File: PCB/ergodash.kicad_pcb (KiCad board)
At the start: 2 copper layers, 149.9 x 127.4 mm, 183 parts, among them J1 5PIN, J2 Conn_01x03, J3 Conn_01x03, J4 GS3, J5 GS3, Q1 IRLML6344TRPbF, SW1 SW_PUSH, SW10 SW_PUSH, SW11 SW_PUSH, SW12 SW_PUSH, SW13 SW_PUSH, SW14 SW_PUSH, SW15 SW_PUSH, SW16 SW_PUSH, SW17 SW_PUSH, SW18 SW_PUSH, SW19 SW_PUSH, SW2 SW_PUSH, SW20 SW_PUSH, SW21 SW_PUSH, SW22 SW_PUSH, SW23 SW_PUSH, SW24 SW_PUSH, SW25 SW_PUSH, SW26 SW_PUSH, SW27 SW_PUSH, SW28 SW_PUSH, SW29 SW_Push, SW3 SW_PUSH, SW30 SW_PUSH, SW31 SW_PUSH, SW32 SW_PUSH, SW33 SW_PUSH, SW34 SW_PUSH, SW35 SW_PUSH, SW36 SW_PUSH, SW37 SW_Push, SW38 SW_PUSH, SW39 SW_PUSH, SW4 SW_PUSH, SW40 SW_PUSH, SW41 SW_PUSH, SW5 SW_PUSH, SW6 SW_PUSH, SW7 SW_PUSH, SW8 SW_PUSH, SW9 SW_PUSH, U1 HOLE, U2 HOLE, U3 ProMicro, U4 HOLE, U5 HOLE, U6 ProMicro, U7 HOLE, U8 HOLE, U9 HOLE

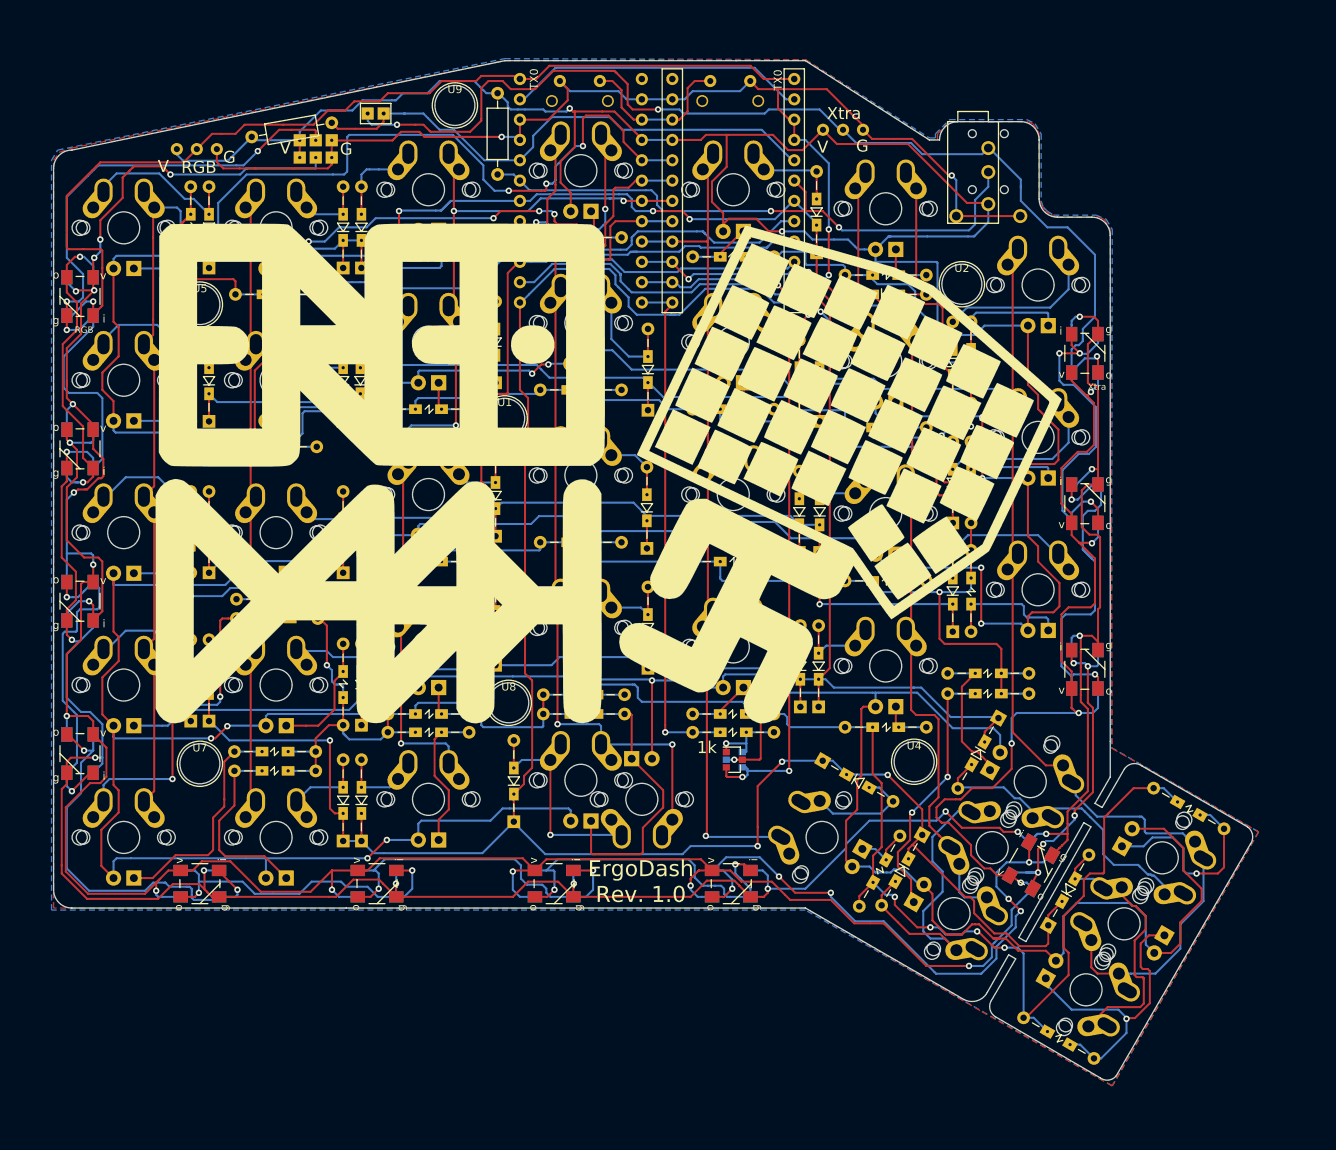
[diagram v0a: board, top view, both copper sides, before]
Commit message: My adpatations added
- Changed TRRS jack to PJ-320A
- Added border and holes for sandwich plateless case
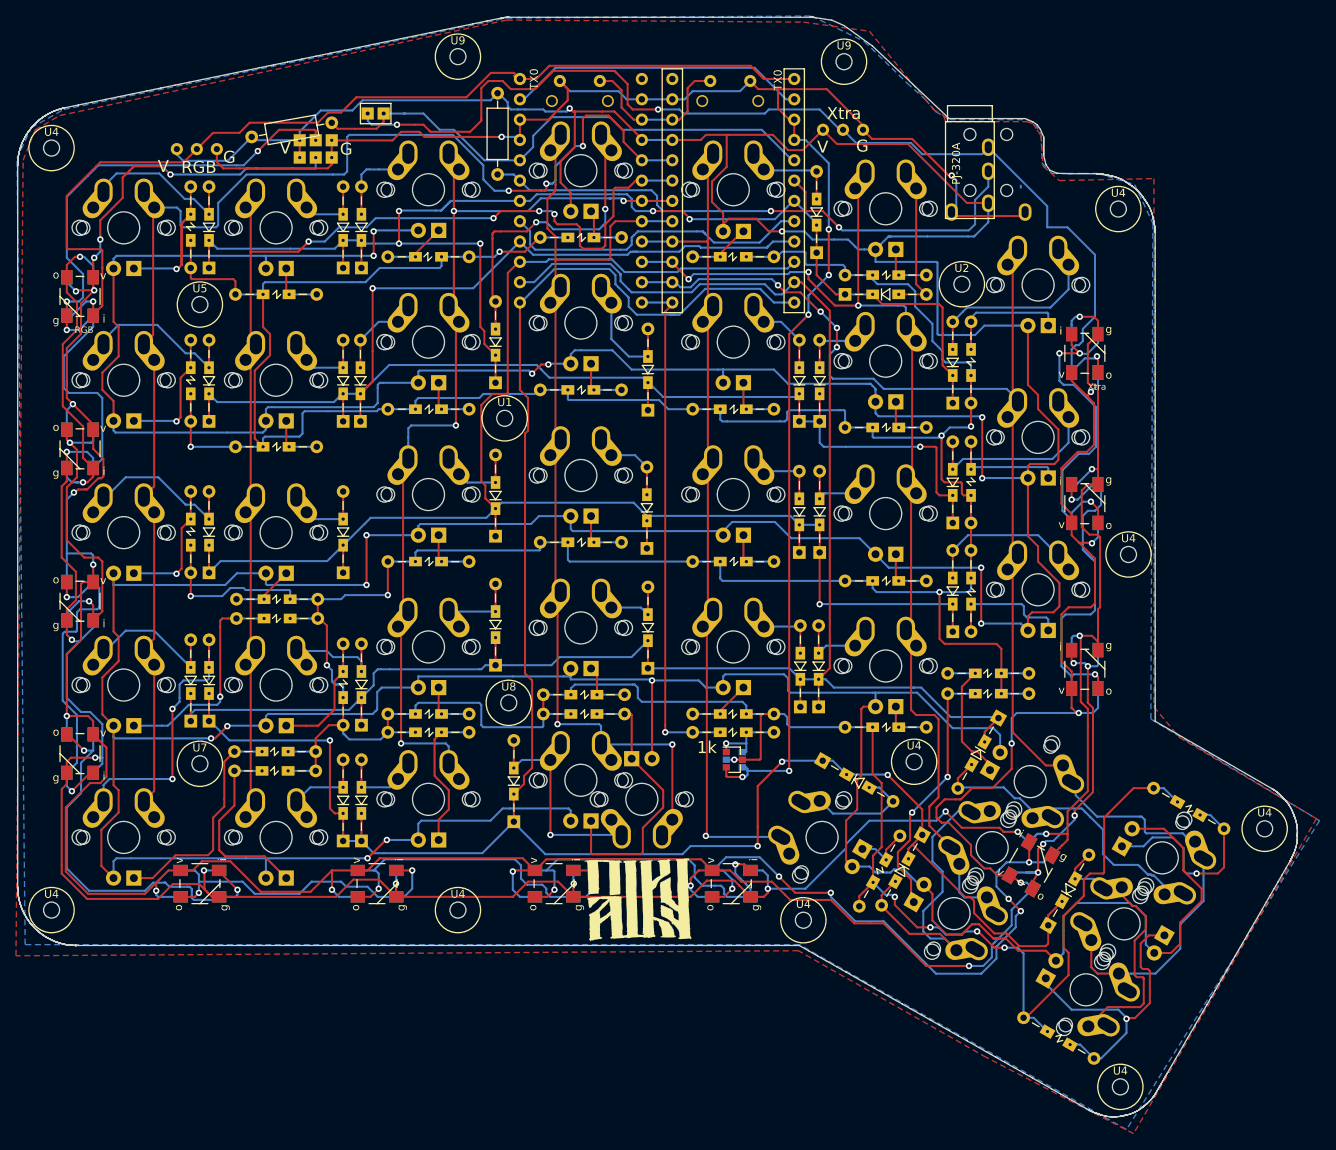
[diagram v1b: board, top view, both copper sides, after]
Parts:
- removed the G*** at (147.6, 88.6)
- removed the G*** at (147.7, 88.5)
- added G***: LOGO, lib:KYLOGO, F.Cu at (151.1, 141.9)
- added G***: LOGO, lib:KYLOGO, B.Cu at (152.0, 141.5)
- added U4: HOLE, lib:hole, F.Cu at (78.0, 48.0)
- added U4: HOLE, lib:hole, F.Cu at (211.3, 55.6)
- added U4: HOLE, lib:hole, F.Cu at (78.0, 143.3)
- added U4: HOLE, lib:hole, F.Cu at (128.8, 143.3)
- added U4: HOLE, lib:hole, F.Cu at (172.0, 144.5)
- added U4: HOLE, lib:hole, F.Cu at (212.6, 98.8)
- added U4: HOLE, lib:hole, F.Cu at (211.6, 165.4)
- added U4: HOLE, lib:hole, F.Cu at (229.6, 133.1)
- added U9: HOLE, lib:hole, F.Cu at (177.0, 37.2)
- J1: footprint library:trrs_jack -> lib:TRRS-PJ-320A-dual
- U1, U2, U4, U5, U7, U8, U9: footprint library:hole -> lib:hole
- moved U9 6.11 mm to (128.8, 36.6)
- turned J1 to 0 degrees
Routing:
- net VCC: track 965.9 -> 964.6 mm
- net /RBG: track 124.4 -> 125.6 mm
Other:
- board size 149.9 x 127.4 mm -> 160 x 137.5 mm
- board text removed: "ErgoDash Rev. 1.0"
